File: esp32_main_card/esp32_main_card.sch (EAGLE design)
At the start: 11 parts, among them J1 09231486921, J2 USB3090-XX-X_REVE, U3 ESP32-DEVKITC-32D

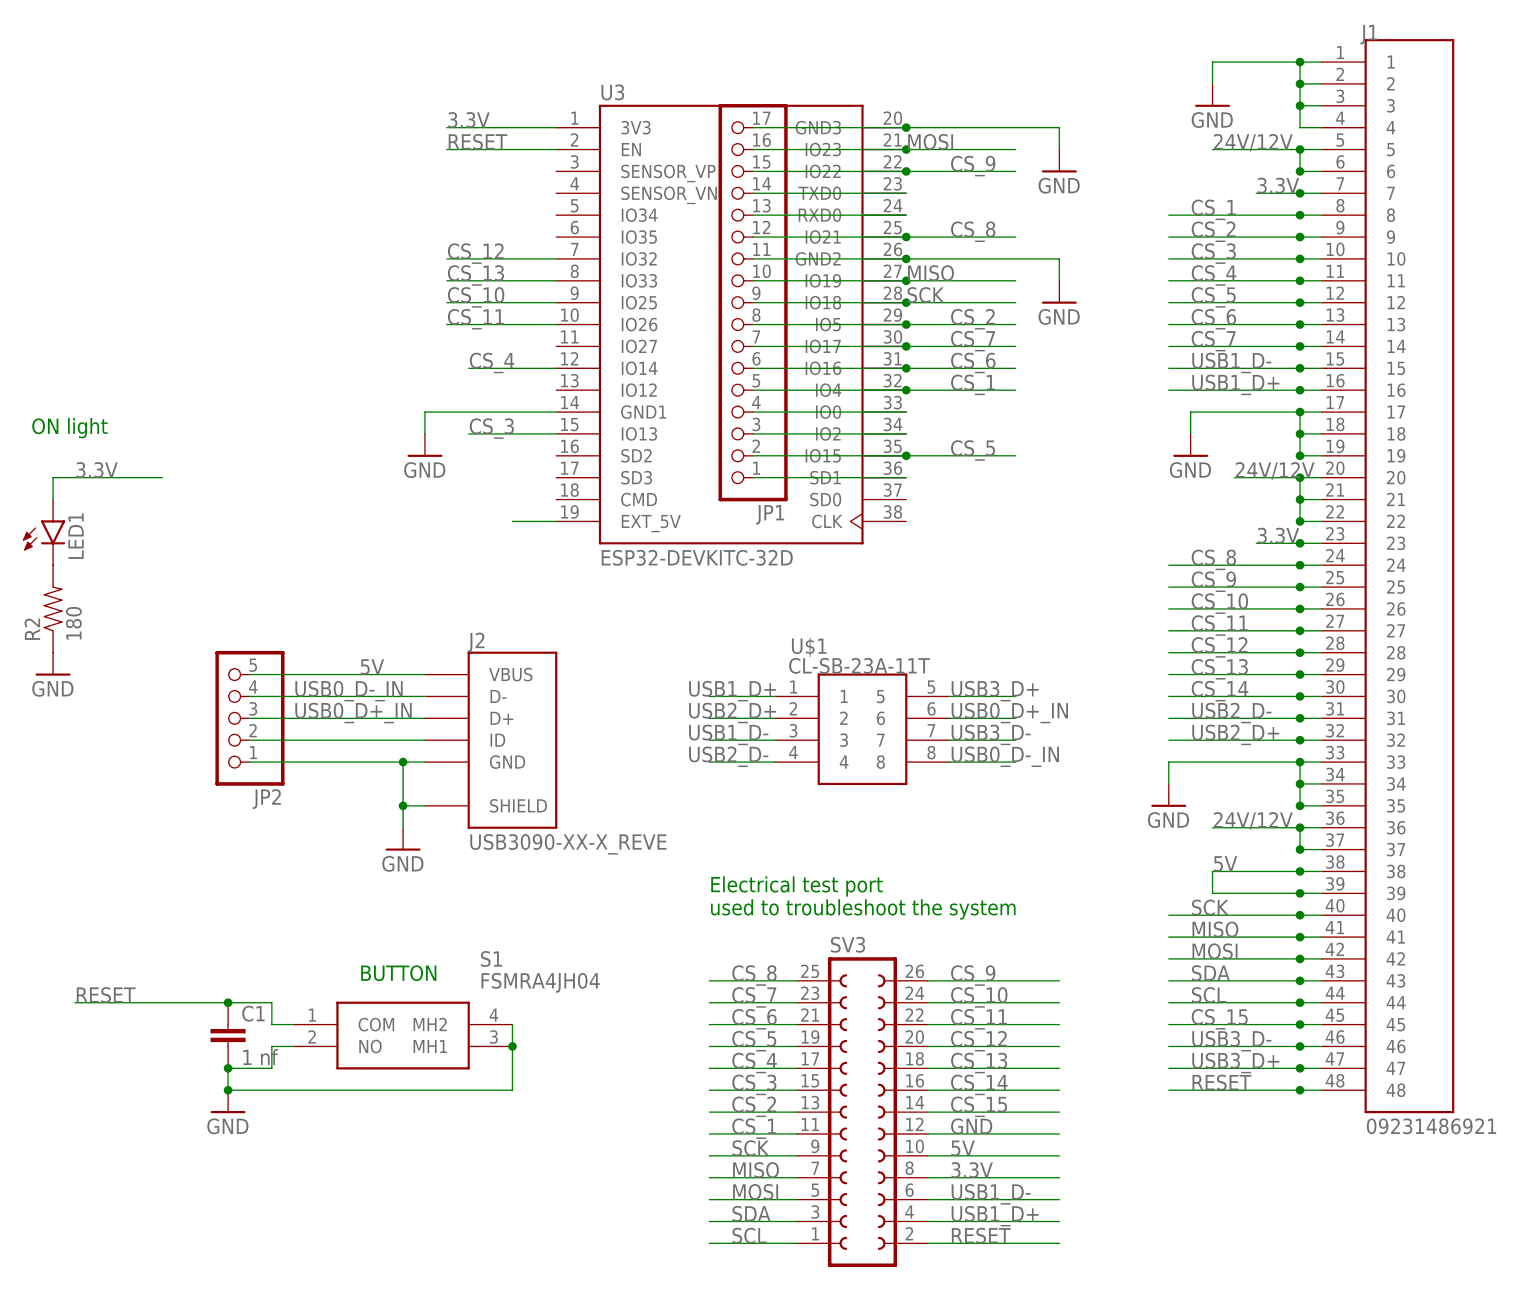
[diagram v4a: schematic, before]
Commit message: updated libraries to generate better bom's
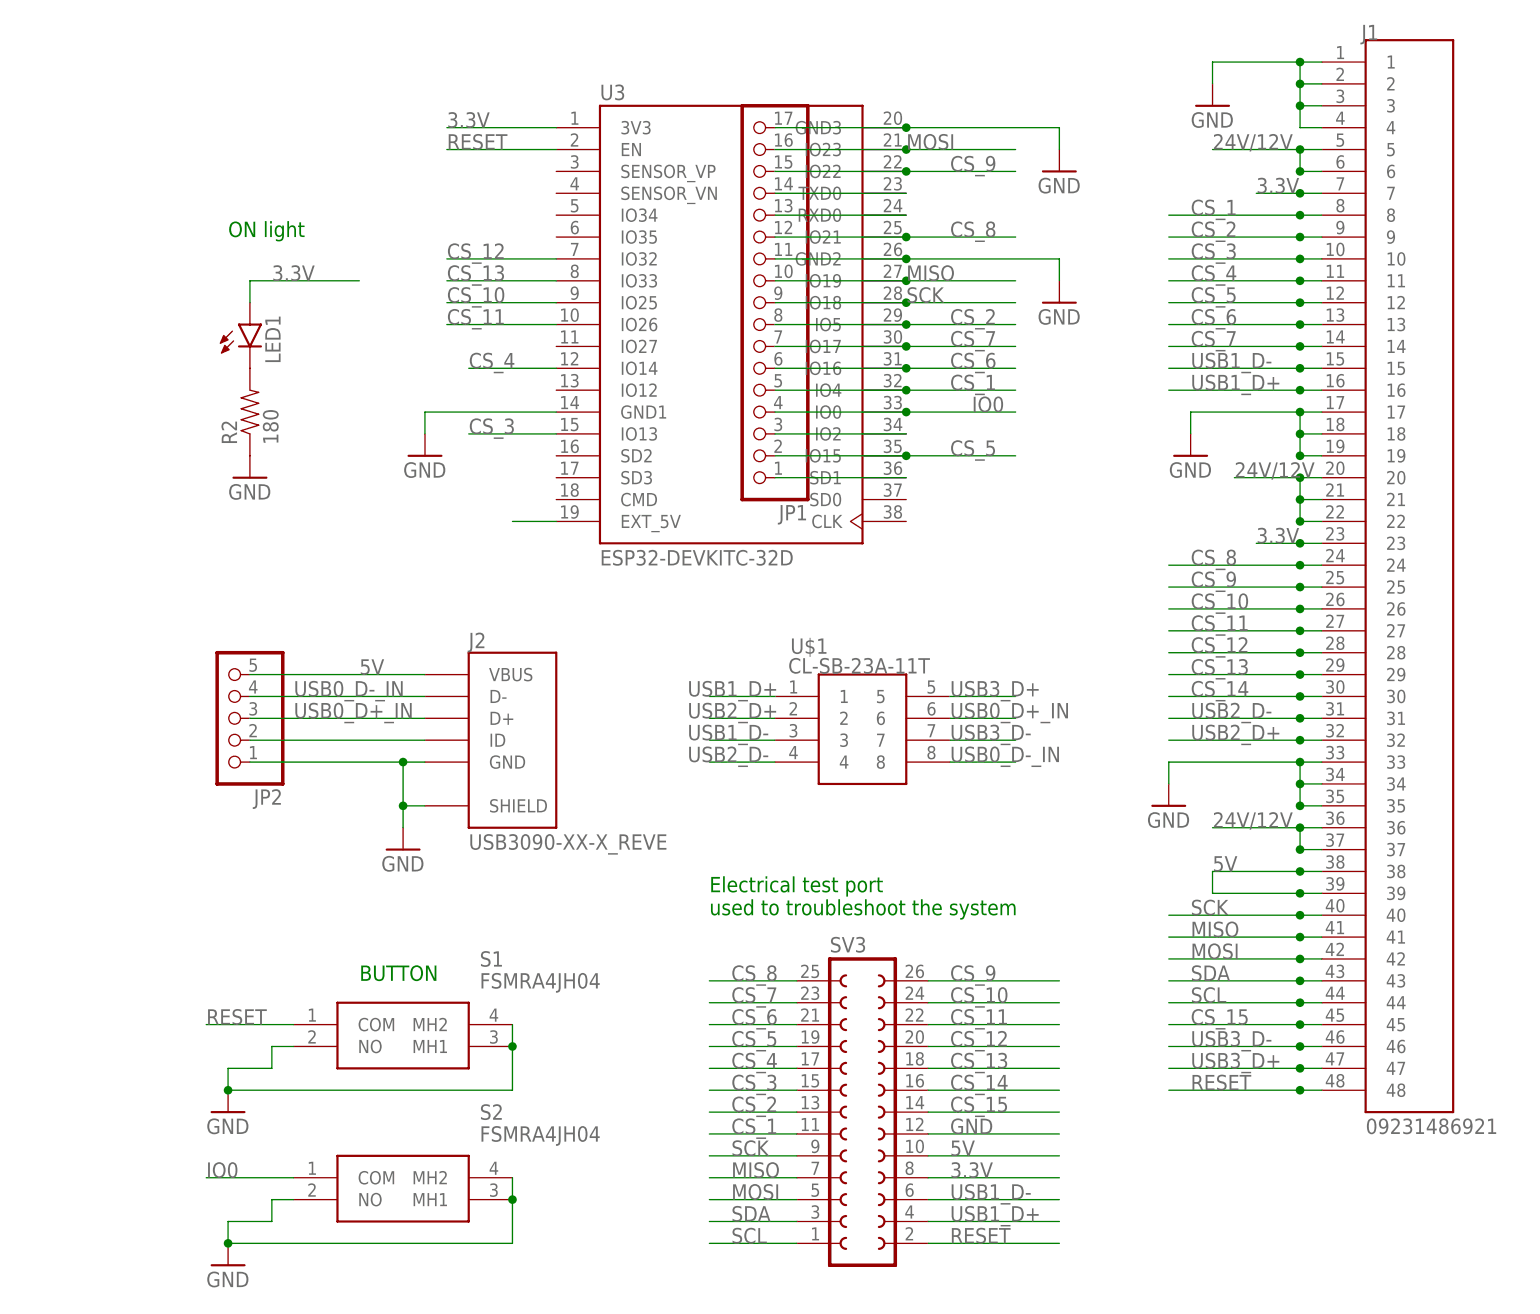
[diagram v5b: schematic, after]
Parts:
- removed C1: 1 nf, SparkFun-Passives:CAP0805
- added S2: FSMRA4JH04, FSMRA4JH04:FSMRA4JH04
- JP1: MANUFACTURER-PART-NUMBER (none) -> SLW-117-01-T-S; PACKAGE (none) -> 2.54 mm header; SIMILAR-COMPONENTS (none) -> https://www.adafruit.com/product/3008
- LED1: COLOR green -> (none); MANUFACTURER-PART-NUMBER (none) -> Generic green 3mm LED; PACKAGE (none) -> none
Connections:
- removed net N$5: JP1.4, U3.IO0
- new net IO0: JP1.4, S2.COM, U3.IO0
- net GND: now also S2.MH1, S2.MH2, S2.NO; no longer C1.2
- net RESET: no longer C1.1
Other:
- moved on the sheet: JP1, LED1, R2

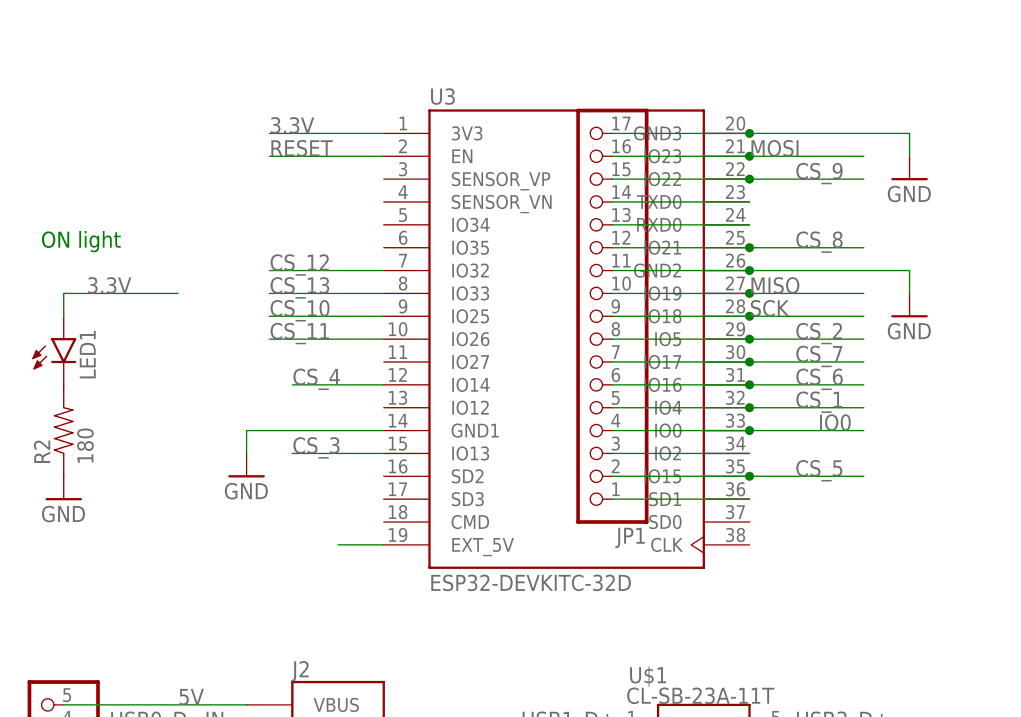
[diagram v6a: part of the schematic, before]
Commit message: added version 2.2 of the main board, which fixes the I2C pin problem
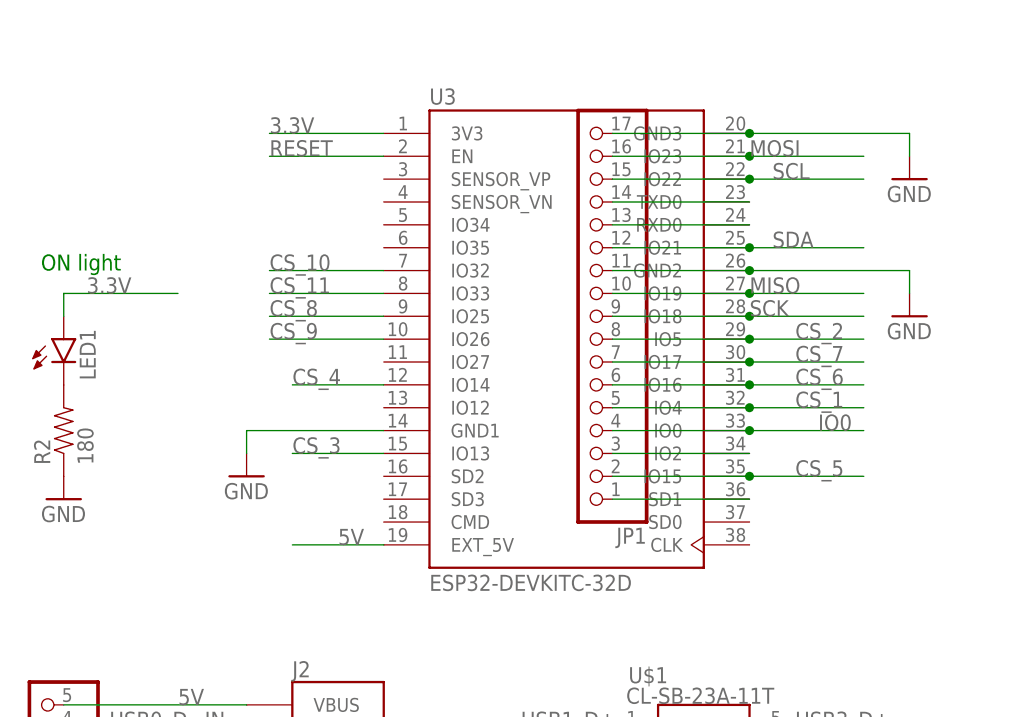
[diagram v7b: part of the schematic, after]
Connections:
- removed net N$10: U3.EXT_5V
- net 5V: now also U3.EXT_5V
- net CS_10: now also U3.IO32; no longer U3.IO25
- net CS_11: now also U3.IO33; no longer U3.IO26
- net CS_12: no longer U3.IO32
- net CS_13: no longer U3.IO33
- net CS_8: now also U3.IO25; no longer JP1.12, U3.IO21
- net CS_9: now also U3.IO26; no longer JP1.15, U3.IO22
- net SCL: now also JP1.15, U3.IO22
- net SDA: now also JP1.12, U3.IO21
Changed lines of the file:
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@@
 used to troubleshoot the system</text>
 <text x="-55.88" y="0" size="1.778" layer="91">BUTTON</text>
-<text x="-71.12" y="86.36" size="1.778" layer="91">ON light</text>
+<text x="-71.12" y="83.82" size="1.778" layer="91">ON light</text>
 </plain>
 <instances>
@@
 </segment>
 <segment>
-<pinref part="U3" gate="G$1" pin="IO21"/>
-<wire x1="7.62" y1="86.36" x2="20.32" y2="86.36" width="0.1524" layer="91"/>
-<label x="12.7" y="86.36" size="1.778" layer="95"/>
-<wire x1="7.62" y1="86.36" x2="-7.62" y2="86.36" width="0.1524" layer="91"/>
-<junction x="7.62" y="86.36"/>
-<pinref part="JP1" gate="G$1" pin="12"/>
-</segment>
-<segment>
 <pinref part="SV3" gate="1" pin="25"/>
 <wire x1="-5.08" y1="0" x2="-15.24" y2="0" width="0.1524" layer="91"/>
 <label x="-12.7" y="0" size="1.778" layer="95"/>
+</segment>
+<segment>
+<pinref part="U3" gate="G$1" pin="IO25"/>
+<wire x1="-33.02" y1="78.74" x2="-45.72" y2="78.74" width="0.1524" layer="91"/>
+<label x="-45.72" y="78.74" size="1.778" layer="95"/>
 </segment>
 </net>
@@
 </segment>
 <segment>
-<pinref part="U3" gate="G$1" pin="IO25"/>
-<wire x1="-33.02" y1="78.74" x2="-45.72" y2="78.74" width="0.1524" layer="91"/>
-<label x="-45.72" y="78.74" size="1.778" layer="95"/>
-</segment>
-<segment>
 <pinref part="SV3" gate="1" pin="24"/>
 <wire x1="25.4" y1="-2.54" x2="10.16" y2="-2.54" width="0.1524" layer="91"/>
 <label x="12.7" y="-2.54" size="1.778" layer="95"/>
+</segment>
+<segment>
+<pinref part="U3" gate="G$1" pin="IO32"/>
+<wire x1="-33.02" y1="83.82" x2="-45.72" y2="83.82" width="0.1524" layer="91"/>
+<label x="-45.72" y="83.82" size="1.778" layer="95"/>
 </segment>
 </net>
@@
 <label x="40.64" y="38.1" size="1.778" layer="95"/>
 <pinref part="J1" gate="G$1" pin="28"/>
-</segment>
-<segment>
-<pinref part="U3" gate="G$1" pin="IO32"/>
-<wire x1="-33.02" y1="83.82" x2="-45.72" y2="83.82" width="0.1524" layer="91"/>
-<label x="-45.72" y="83.82" size="1.778" layer="95"/>
 </segment>
 <segment>
@@
 <pinref part="JP2" gate="A" pin="5"/>
 </segment>
+<segment>
+<pinref part="U3" gate="G$1" pin="EXT_5V"/>
+<wire x1="-33.02" y1="53.34" x2="-43.18" y2="53.34" width="0.1524" layer="91"/>
+<label x="-38.1" y="53.34" size="1.778" layer="95"/>
+</segment>
 </net>
 <net name="SCK" class="0">
@@
 <pinref part="SV3" gate="1" pin="3"/>
 </segment>
+<segment>
+<pinref part="U3" gate="G$1" pin="IO21"/>
+<wire x1="7.62" y1="86.36" x2="-7.62" y2="86.36" width="0.1524" layer="91"/>
+<pinref part="JP1" gate="G$1" pin="12"/>
+<wire x1="7.62" y1="86.36" x2="20.32" y2="86.36" width="0.1524" layer="91"/>
+<junction x="7.62" y="86.36"/>
+<label x="10.16" y="86.36" size="1.778" layer="95"/>
+</segment>
 </net>
 <net name="SCL" class="0">
@@
 <label x="-12.7" y="-30.48" size="1.778" layer="95"/>
 <pinref part="SV3" gate="1" pin="1"/>
+</segment>
+<segment>
+<pinref part="U3" gate="G$1" pin="IO22"/>
+<pinref part="JP1" gate="G$1" pin="15"/>
+<wire x1="7.62" y1="93.98" x2="-7.62" y2="93.98" width="0.1524" layer="91"/>
+<wire x1="7.62" y1="93.98" x2="20.32" y2="93.98" width="0.1524" layer="91"/>
+<junction x="7.62" y="93.98"/>
+<label x="10.16" y="93.98" size="1.778" layer="95"/>
 </segment>
 </net>
@@
 </segment>
 <segment>
-<pinref part="U3" gate="G$1" pin="IO33"/>
-<wire x1="-33.02" y1="81.28" x2="-45.72" y2="81.28" width="0.1524" layer="91"/>
-<label x="-45.72" y="81.28" size="1.778" layer="95"/>
-</segment>
-<segment>
 <pinref part="SV3" gate="1" pin="18"/>
 <wire x1="10.16" y1="-10.16" x2="25.4" y2="-10.16" width="0.1524" layer="91"/>
@@
 </segment>
 <segment>
-<pinref part="U3" gate="G$1" pin="IO26"/>
-<wire x1="-33.02" y1="76.2" x2="-45.72" y2="76.2" width="0.1524" layer="91"/>
-<label x="-45.72" y="76.2" size="1.778" layer="95"/>
-</segment>
-<segment>
 <pinref part="SV3" gate="1" pin="22"/>
 <wire x1="10.16" y1="-5.08" x2="25.4" y2="-5.08" width="0.1524" layer="91"/>
 <label x="12.7" y="-5.08" size="1.778" layer="95"/>
+</segment>
+<segment>
+<pinref part="U3" gate="G$1" pin="IO33"/>
+<wire x1="-33.02" y1="81.28" x2="-45.72" y2="81.28" width="0.1524" layer="91"/>
+<label x="-45.72" y="81.28" size="1.778" layer="95"/>
 </segment>
 </net>
@@
 </segment>
 <segment>
-<pinref part="U3" gate="G$1" pin="IO22"/>
-<wire x1="7.62" y1="93.98" x2="20.32" y2="93.98" width="0.1524" layer="91"/>
-<label x="12.7" y="93.98" size="1.778" layer="95"/>
-<wire x1="7.62" y1="93.98" x2="-7.62" y2="93.98" width="0.1524" layer="91"/>
-<junction x="7.62" y="93.98"/>
-<pinref part="JP1" gate="G$1" pin="15"/>
-</segment>
-<segment>
 <pinref part="SV3" gate="1" pin="26"/>
 <wire x1="10.16" y1="0" x2="25.4" y2="0" width="0.1524" layer="91"/>
 <label x="12.7" y="0" size="1.778" layer="95"/>
+</segment>
+<segment>
+<pinref part="U3" gate="G$1" pin="IO26"/>
+<wire x1="-33.02" y1="76.2" x2="-45.72" y2="76.2" width="0.1524" layer="91"/>
+<label x="-45.72" y="76.2" size="1.778" layer="95"/>
 </segment>
 </net>
@@
 </segment>
 </net>
-<net name="N$10" class="0">
-<segment>
-<pinref part="U3" gate="G$1" pin="EXT_5V"/>
-<wire x1="-33.02" y1="53.34" x2="-38.1" y2="53.34" width="0.1524" layer="91"/>
-</segment>
-</net>
